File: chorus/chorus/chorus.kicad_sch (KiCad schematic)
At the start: 19 parts, among them J1 IN, J3 Jack-DC, J4 OUT, SW1 SW_3PDT_x3, U2 TL074, U3 TL074, U5 LM7805, U6 TL072, U8 TLE2426xLP

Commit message: add output buffer
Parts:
- added C?: 100u, symbol Device:C_Polarized
- added R?: 10k, symbol Device:R
- added U?: LM13700, symbol Amplifier_Operational:LM13700
- R13: value 220 -> 2.2k
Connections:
- net GND: now also R?.2
- net at R26.1, R3.2, U3.1: now also U?.10; no longer SW1.7 (A)
- new net: C?.2, SW1.7 (A)
- new net: C?.1, R?.1, U?.9
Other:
- note added: "Output buffer capable of 20mA"
- note added: "TODO: IC power filter caps"
- note added: "TODO: addative, not blended"
- note added: "TODO: is 2.2K LED current limitter bright enough?"
- note added: "sum half full dry signal plus half wet signal (filtered + delayed signal plus remaining signal) TODO: wet/dry mix?"
- note removed: "TODO: use other LM13700 buffer on output?"
- note removed: "sum half dry signal plus half wet signal"
- company: (none) -> rabidaudio
- title: (none) -> Bass Chorus
- moved on the sheet: J1, J4, R1, R2, R26, R3, R4, R6, R7, R_FLANGE1, SW1A, SW1C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

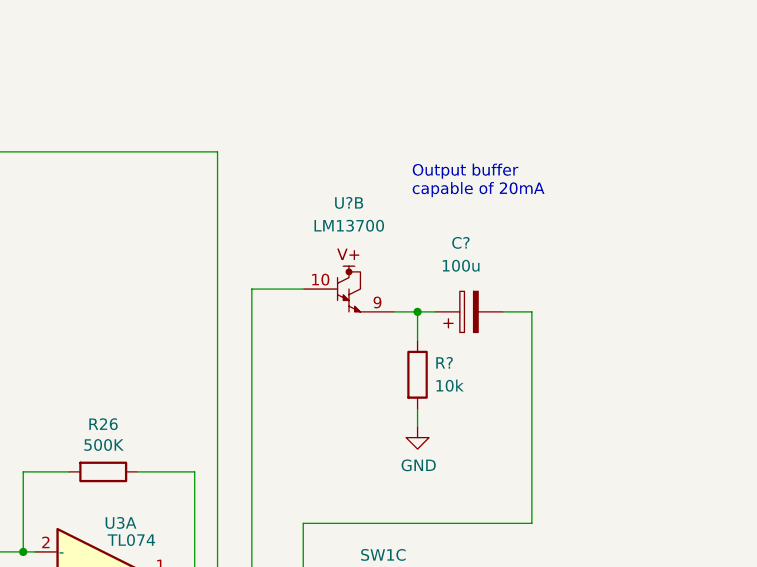
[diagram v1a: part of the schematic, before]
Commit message: swap wet-dry direction to be more intuitive
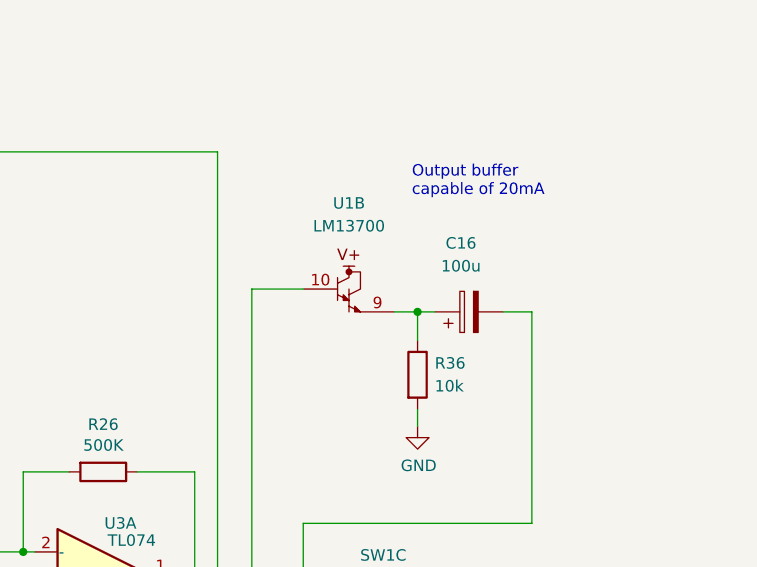
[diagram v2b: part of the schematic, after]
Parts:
- gave numbers to parts that had none: 3
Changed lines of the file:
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@@
   (symbol (lib_id "Amplifier_Operational:LM13700") (at 254 100.33 0) (unit 2)
     (in_bom yes) (on_board yes) (fields_autoplaced)
-    (property "Reference" "U?" (id 0) (at 251.46 90.805 0))
+    (property "Reference" "U1" (id 0) (at 251.46 90.805 0))
     (property "Value" "LM13700" (id 1) (at 251.46 93.345 0))
     (property "Footprint" "" (id 2) (at 246.38 99.695 0)
@@
   (symbol (lib_id "Device:C_Polarized") (at 264.795 102.87 90) (unit 1)
     (in_bom yes) (on_board yes) (fields_autoplaced)
-    (property "Reference" "C?" (id 0) (at 263.906 95.25 90))
+    (property "Reference" "C16" (id 0) (at 263.906 95.25 90))
     (property "Value" "100u" (id 1) (at 263.906 97.79 90))
     (property "Footprint" "" (id 2) (at 268.605 101.9048 0)
@@
   (symbol (lib_id "Device:R") (at 259.08 109.855 0) (unit 1)
     (in_bom yes) (on_board yes) (fields_autoplaced)
-    (property "Reference" "R?" (id 0) (at 260.985 108.5849 0)
+    (property "Reference" "R36" (id 0) (at 260.985 108.5849 0)
       (effects (font (size 1.27 1.27)) (justify left))
     )
@@
   (symbol (lib_id "power:GND") (at 259.08 115.57 0) (unit 1)
     (in_bom yes) (on_board yes)
-    (property "Reference" "#PWR?" (id 0) (at 259.08 121.92 0)
+    (property "Reference" "#PWR0101" (id 0) (at 259.08 121.92 0)
       (effects (font (size 1.27 1.27)) hide)
     )
@@
       (reference "#PWR06") (unit 1) (value "GNDA") (footprint "")
     )
+    (path "/ef5bd4b7-e497-4e8f-bf39-267d25b8e837"
+      (reference "#PWR0101") (unit 1) (value "GND") (footprint "")
+    )
     (path "/00000000-0000-0000-0000-0000628336f3/d0da2238-d6a4-422f-a4e1-2ce398dfd4c9"
       (reference "#PWR0103") (unit 1) (value "GNDA") (footprint "")
@@
       (reference "#PWR0146") (unit 1) (value "GNDA") (footprint "")
     )
-    (path "/ef5bd4b7-e497-4e8f-bf39-267d25b8e837"
-      (reference "#PWR?") (unit 1) (value "GND") (footprint "")
-    )
     (path "/00000000-0000-0000-0000-00006325a0b8/00000000-0000-0000-0000-000062b60b28"
       (reference "C1") (unit 1) (value "10n") (footprint "")
@@
     )
     (path "/52079f04-5edf-4394-a4e0-cdbdc34d27d4"
-      (reference "C?") (unit 1) (value "100u") (footprint "")
+      (reference "C16") (unit 1) (value "100u") (footprint "")
     )
     (path "/00000000-0000-0000-0000-000062f7b2b4/00000000-0000-0000-0000-0000631f8c21"
@@
     )
     (path "/e7f7a979-4af5-4886-9e1b-d33551674310"
-      (reference "R?") (unit 1) (value "10k") (footprint "")
+      (reference "R36") (unit 1) (value "10k") (footprint "")
     )
     (path "/00000000-0000-0000-0000-00006325a0b8/00000000-0000-0000-0000-000062ae72d8"
@@
       (reference "U1") (unit 1) (value "LM13700") (footprint "kicad-legacy/kicad-footprints/Package_DIP.pretty:DIP-16_W7.62mm")
     )
+    (path "/3ff7fac8-d636-4cb9-8d46-24789ada3aa8"
+      (reference "U1") (unit 2) (value "LM13700") (footprint "")
+    )
     (path "/00000000-0000-0000-0000-000062f7b2b4/00000000-0000-0000-0000-000062f9d2e5"
       (reference "U1") (unit 3) (value "LM13700") (footprint "kicad-legacy/kicad-footprints/Package_DIP.pretty:DIP-16_W7.62mm")
@@
       (reference "U11") (unit 2) (value "TL072") (footprint "kicad-legacy/Housings_DIP.pretty:DIP-8_W7.62mm")
     )
-    (path "/3ff7fac8-d636-4cb9-8d46-24789ada3aa8"
-      (reference "U?") (unit 2) (value "LM13700") (footprint "")
-    )
-  )
+  )
